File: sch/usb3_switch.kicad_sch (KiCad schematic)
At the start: 33 parts, among them J3 USB3_A, J4 USB_C_Receptacle, J5 USB3_A, K1 Relay_DPDT_Panasonic_AGQ200A4H, Q1 2N7002P, SW1 C2689642, U4 FSUSB42MUX

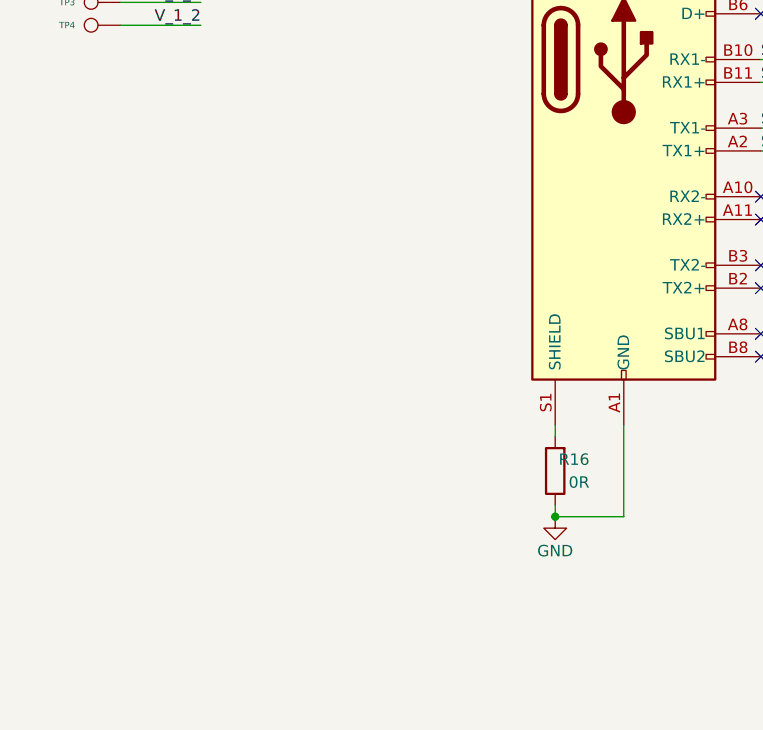
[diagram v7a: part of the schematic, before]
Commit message: added more DNF components for easy debugging
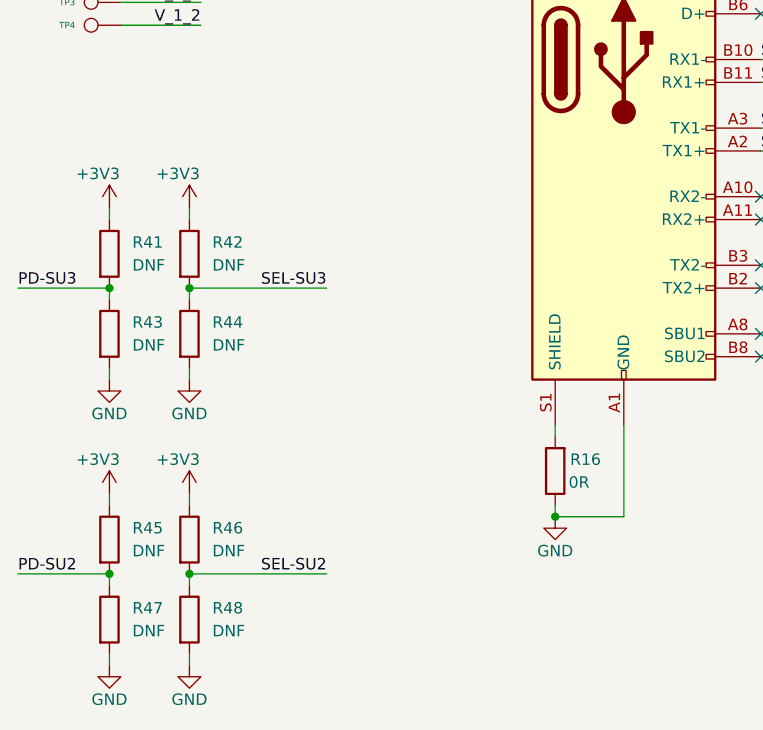
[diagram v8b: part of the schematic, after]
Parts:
- added R41, R42, R43, R44, R45, R46, R47, R48: DNF, Resistor_SMD:R_0402_1005Metric_Pad0.72x0.64mm_HandSolder, symbol Device:R
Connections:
- net +3V3: now also R41.1, R42.1, R45.1, R46.1
- net GND: now also R43.2, R44.2, R47.2, R48.2
- net PD-SU2: now also R45.2, R47.1
- net PD-SU3: now also R41.2, R43.1
- net SEL-SU2: now also R46.2, R48.1
- net SEL-SU3: now also R42.2, R44.1
